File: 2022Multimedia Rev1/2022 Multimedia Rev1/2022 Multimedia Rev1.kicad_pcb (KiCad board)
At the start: 2 copper layers, 124.5 x 87.1 mm, 24 parts, among them U1 OKI, U2 OKI, U3 BDJ2GA5WEFJ, U4 TM4C129E_Launchpad

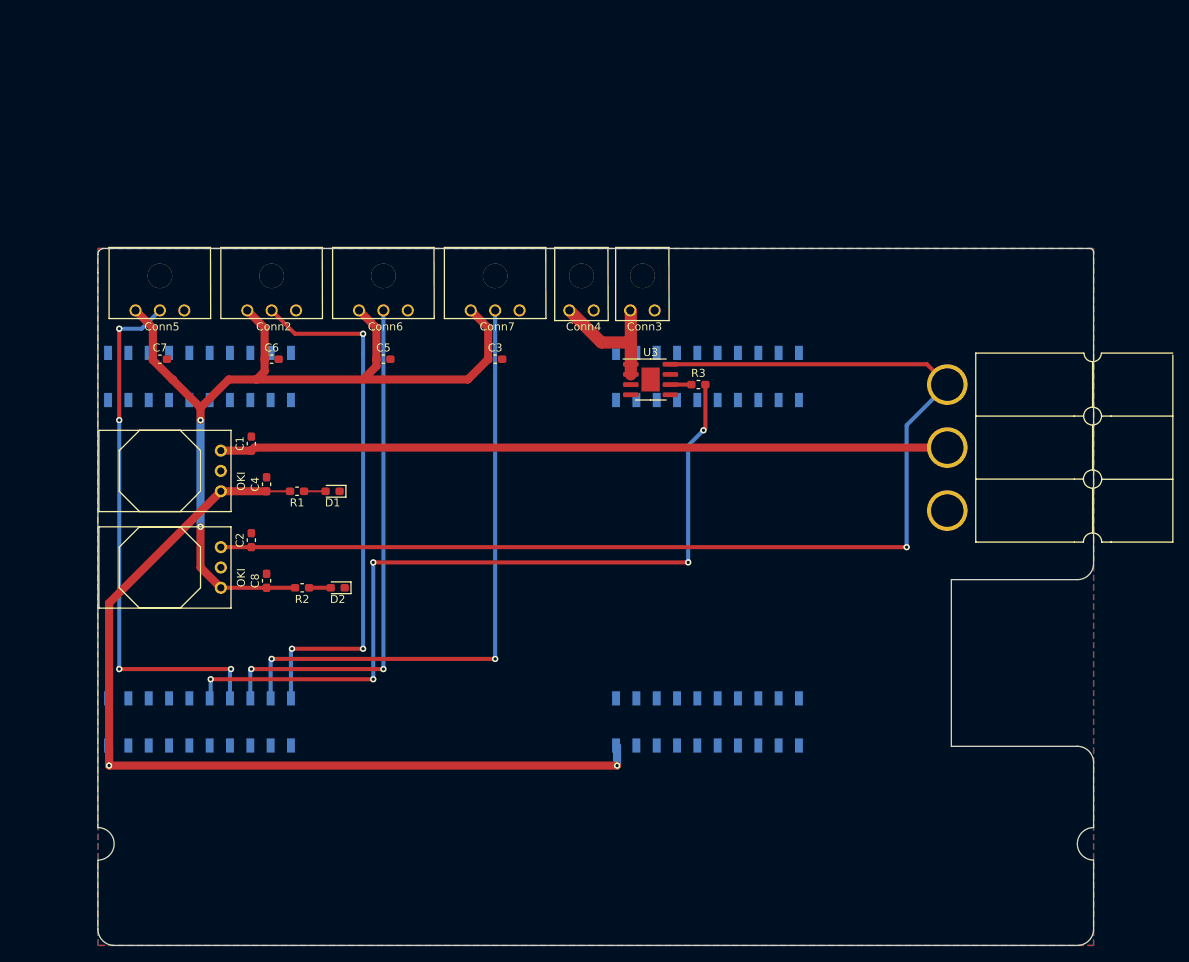
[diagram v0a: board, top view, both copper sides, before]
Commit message: Finished layout and silkscreens
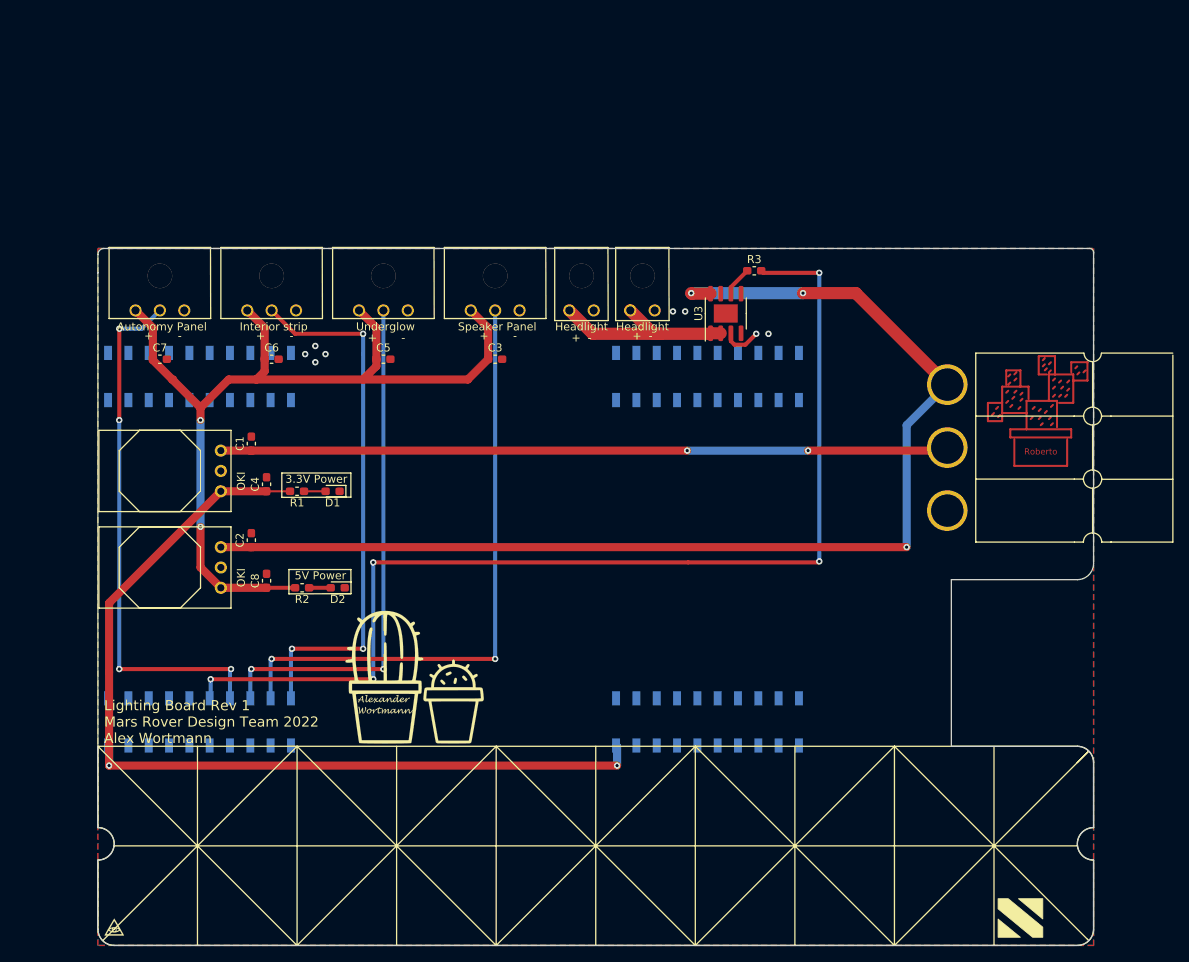
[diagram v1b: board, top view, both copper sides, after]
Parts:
- added G***: LOGO, Silk Screens:SmolCactus, F.Cu at (156.7, 108.5)
- added G***: LOGO, Silk Screens:PricklySig, F.Cu at (148.1, 105.2)
- added G***: LOGO, MRDT_Silkscreens:2_Nothing_3mm, F.Cu at (114.3, 136.4)
- Autonomy Panel: renamed from Conn5
- Interior strip: renamed from Conn2
- Speaker Panel: renamed from Conn7
- moved R3 15.8 mm to (194.3, 54.4)
- moved U3 12.5 mm to (190.8, 59.7), turned to 90 degrees
- renumbered Conn4 to Headlight, Conn3 to Headlight, Conn6 to Underglow
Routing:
- net (no net): track 0.00 -> 105.9 mm
- net HeadlightToggle: track 99.8 -> 136.6 mm
- net Net-(Conn3-Pad1): track 17.4 -> 25.3 mm
- net GND: track 0.00 -> 4.90 mm, vias 0 -> 8
- net +12VA: track 143.8 -> 147.3 mm, vias 1 -> 3
- net Net-(R3-Pad1): track 2.62 -> 3.71 mm
- net +12L: vias 0 -> 2
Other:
- board text added: "+ -"
- board text added: "3.3V Power"
- board text added: "5V Power"
- board text added: "Lighting Board Rev 1 Mars Rover Design Team 2022 Alex Wortmann"
- board text added: "Roberto"

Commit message: Changed andersons
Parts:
- added G***: LOGO, MRDT_Silkscreens:0_MRDT_Logo_40mm, F.Cu at (214.9, 74.2)
- moved Conn1 88.4 mm to (130.3, 78.0), turned to 0 degrees
- moved G*** 31.5 mm to (188.2, 108.5)
- moved G*** 31.2 mm to (179.3, 105.2)
- moved C1 26.9 mm to (158.4, 75.5)
- moved C2 26.9 mm to (158.4, 87.5)
- moved C4 26.9 mm to (160.3, 80.5)
- moved C8 26.9 mm to (160.3, 92.6)
- moved D1 26.9 mm to (168.5, 81.4)
- moved R1 26.9 mm to (164.1, 81.4)
- moved R2 26.9 mm to (164.7, 93.5)
- moved U1 26.9 mm to (154.6, 76.3)
- moved U2 26.9 mm to (154.6, 88.4)
- moved D2 26.9 mm to (169.2, 93.5)
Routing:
- net +12L: track 94.5 -> 35.6 mm, vias 2 -> 0
- net +12VA: track 147.3 -> 130.4 mm, vias 3 -> 2
- net Net-(R3-Pad1): track 3.71 -> 5.20 mm
- net +5V: track 114.1 -> 115.1 mm, vias 2 -> 1
- net +3V3: track 117.4 -> 116.6 mm, vias 2 -> 4
- net HeadlightToggle: track 136.6 -> 136.7 mm, vias 5 -> 3

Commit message: Rev2 Done
Need to do Gerbs
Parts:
- removed C3, C8: 10uF, Capacitor_SMD:C_0603_1608Metric_Pad1.05x0.95mm_HandSolder
- removed C6: 10 uF, Capacitor_SMD:C_0603_1608Metric_Pad1.05x0.95mm_HandSolder
- removed G***: LOGO, MRDT_Silkscreens:0_MRDT_Logo_40mm
- removed G***: LOGO, Silk Screens:SmolCactus
- removed G***: LOGO, Silk Screens:PricklySig
- removed G***: LOGO, MRDT_Silkscreens:2_Nothing_3mm
- removed Headlight: Lights2, MRDT_Connectors:MOLEX_uF_S_02_Horizontal
- removed Headlight: Lights, MRDT_Connectors:MOLEX_uF_S_02_Horizontal
- removed Interior strip: Interior Lights, MRDT_Connectors:MOLEX_uF_S_03_Horizontal
- removed R3: 480, Resistor_SMD:R_0603_1608Metric_Pad1.05x0.95mm_HandSolder
- removed Speaker Panel: Speaker Panel, MRDT_Connectors:MOLEX_uF_S_03_Horizontal
- removed Underglow: Underglow, MRDT_Connectors:MOLEX_uF_S_03_Horizontal
- added C10: 10 uF, Capacitor_SMD:C_0603_1608Metric_Pad1.05x0.95mm_HandSolder, F.Cu at (158.1, 74.4)
- added C9: 10 uF, Capacitor_SMD:C_0603_1608Metric_Pad1.05x0.95mm_HandSolder, F.Cu at (170.8, 74.4)
- added Conn2: Wirrly Light, MRDT_Connectors:Square_Anderson_2_H_Side_By_Side, F.Cu at (152.4, 69.8)
- added Conn3: Headlight, MRDT_Connectors:Square_Anderson_2_H_Side_By_Side, F.Cu at (170.2, 69.8)
- Conn1: footprint MRDT_Connectors:Anderson_3_Horizontal_Side_by_Side -> MRDT_Connectors:Square_Anderson_3_H_Side_By_Side
- Conn5: renamed from Autonomy Panel
- R1: value 47 -> 120
- R2: value 100 -> 300
- U1, U2: moved to B.Cu
- moved C4 33.2 mm to (135.0, 102.1), turned to 180 degrees
- moved C1 31.8 mm to (135.0, 97.0), turned to 180 degrees
- moved U3 31.3 mm to (164.3, 76.3), turned to 0 degrees
- moved U1 25.0 mm to (140.5, 97.0)
- moved C2 19.3 mm to (144.9, 73.7), turned to 0 degrees
- moved U2 15.4 mm to (144.0, 77.2), turned to 180 degrees
- moved D2 15.2 mm to (156.5, 85.1)
- moved R2 15.2 mm to (152.0, 85.1)
- moved D1 14.7 mm to (156.8, 90.3)
- moved R1 14.7 mm to (152.4, 90.3)
- moved C5 12.9 mm to (138.1, 73.7), turned to 180 degrees
- moved Conn1 8.88 mm to (130.2, 86.9)
- moved Conn5 5.72 mm to (125.7, 60.3)
- moved C7 3.60 mm to (123.6, 64.8)
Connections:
- U3 pad 5: (no net) -> HeadlightToggle
- U3 pad 6: Net-(R3-Pad1) -> (no net)
- U4 pad PA6: UnderglowNeoPixel -> Net-(U4-PadPA6)
- U4 pad PD7: AutopanelNeoPixel -> Net-(U4-PadPD7)
- U4 pad PF1: Net-(U4-PadPF1) -> AutopanelNeoPixel
- U4 pad PM4: SpeakerNeoPixel -> Net-(U4-PadPM4)
- U4 pad PM5: InteriorNeoPixel -> Net-(U4-PadPM5)
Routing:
- net SpeakerNeoPixel: track 76.5 -> 0.00 mm, vias 2 -> 0
- net +5V: track 115.1 -> 45.2 mm, vias 1 -> 2
- net InteriorNeoPixel: track 67.2 -> 0.00 mm, vias 3 -> 0
- net +12VA: track 130.4 -> 63.6 mm, vias 2 -> 1
- net UnderglowNeoPixel: track 65.1 -> 0.00 mm, vias 2 -> 0
- net HeadlightToggle: track 136.7 -> 75.9 mm, vias 3 -> 1
- net AutopanelNeoPixel: track 66.3 -> 22.6 mm, vias 4 -> 1
- net +12L: track 35.6 -> 16.3 mm
- net +3V3: track 116.6 -> 100.1 mm, vias 4 -> 1
- net Net-(C10-Pad1): track 25.3 -> 9.03 mm
- net Net-(R3-Pad1): track 5.20 -> 0.00 mm
- net GND: track 4.90 -> 0.00 mm, vias 8 -> 0
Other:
- board text added: "Lighting Board Rev 2 Mars Rover Design Team 2022 Alex Wortmann"
- board text removed: "Lighting Board Rev 1 Mars Rover Design Team 2022 Alex Wortmann"

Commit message: Finished rev2
gerbs and all, except bom
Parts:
- removed C2, C5: 10 uF, Capacitor_SMD:C_0603_1608Metric_Pad1.05x0.95mm_HandSolder
- removed Conn5: Auto Panel, MRDT_Connectors:MOLEX_uF_S_03_Horizontal
- added Conn4: AndersonPP, MRDT_Connectors:Square_Anderson_2_H_Side_By_Side, F.Cu at (161.1, 51.2)
- added Data: Neopixel Power, MRDT_Connectors:MOLEX_uF_S_02_Horizontal, F.Cu at (171.4, 41.5)
- added G***: LOGO, MRDT_Silkscreens:0_MRDT_Logo_50mm, F.Cu at (206.8, 59.4)
- added G***: LOGO, MRDT_Silkscreens:SmolCactus, F.Cu at (205.2, 95.5)
- added G***: LOGO, MRDT_Silkscreens:PricklySig, F.Cu at (196.1, 92.2)
- U1: value OKI -> TSR1-2433; footprint MRDT_Devices:OKI_Horizontal -> MRDT_Devices:TSR_1-2433; moved to F.Cu
- U2: value OKI -> China5V8ABuck; footprint MRDT_Devices:OKI_Horizontal -> 2022 Multimedia Rev1:China5V8ABuck; moved to F.Cu
- moved C9 39.9 mm to (132.7, 62.5)
- moved U3 39.3 mm to (129.9, 57.3), turned to 270 degrees
- moved C7 34.3 mm to (156.2, 54.4)
- moved C4 33.1 mm to (168.0, 105.2), turned to 0 degrees
- moved Conn3 32.6 mm to (143.5, 51.2)
- moved Conn2 32.5 mm to (125.8, 51.3)
- moved C10 30.4 mm to (134.1, 55.7), turned to 270 degrees
- moved D2 27.7 mm to (182.1, 95.5)
- moved R2 27.7 mm to (177.7, 95.5)
- moved D1 27.3 mm to (182.0, 101.0)
- moved R1 27.3 mm to (177.5, 101.0)
- moved U2 23.2 mm to (147.3, 54.2), turned to 0 degrees
- moved U1 20.1 mm to (159.5, 103.4), turned to 0 degrees
- moved C1 16.8 mm to (150.1, 104.3), turned to 90 degrees
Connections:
- U2 pad 3: +5V -> GND
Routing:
- net AutopanelNeoPixel: track 22.6 -> 88.0 mm
- net +12VA: track 63.6 -> 0.00 mm, vias 1 -> 0
- net +5V: track 45.2 -> 7.66 mm, vias 2 -> 0
- net +12L: track 16.3 -> 49.2 mm
- net HeadlightToggle: track 75.9 -> 51.8 mm, vias 1 -> 5
- net +3V3: track 100.1 -> 92.7 mm
- net Net-(C10-Pad1): track 9.03 -> 8.43 mm
- net GND: vias 0 -> 19
- added copper zone on F.Cu, net +12VA
- added copper zone on F.Cu, net +5V
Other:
- board size 124.5 x 87.1 mm -> 124.5 x 105.9 mm
- board text added: "GND"
- board text removed: "+ -"
